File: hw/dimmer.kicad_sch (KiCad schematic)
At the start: 40 parts, among them J4 Screw_Terminal_01x02, Q10 MMBT3904, Q11 MMBT3906, Q13 IPN80R900P7, Q14 IPN80R900P7, Q9 MMBT3904, U2 PC817XI, U3 H11L1SR2M, U4 PC817XI

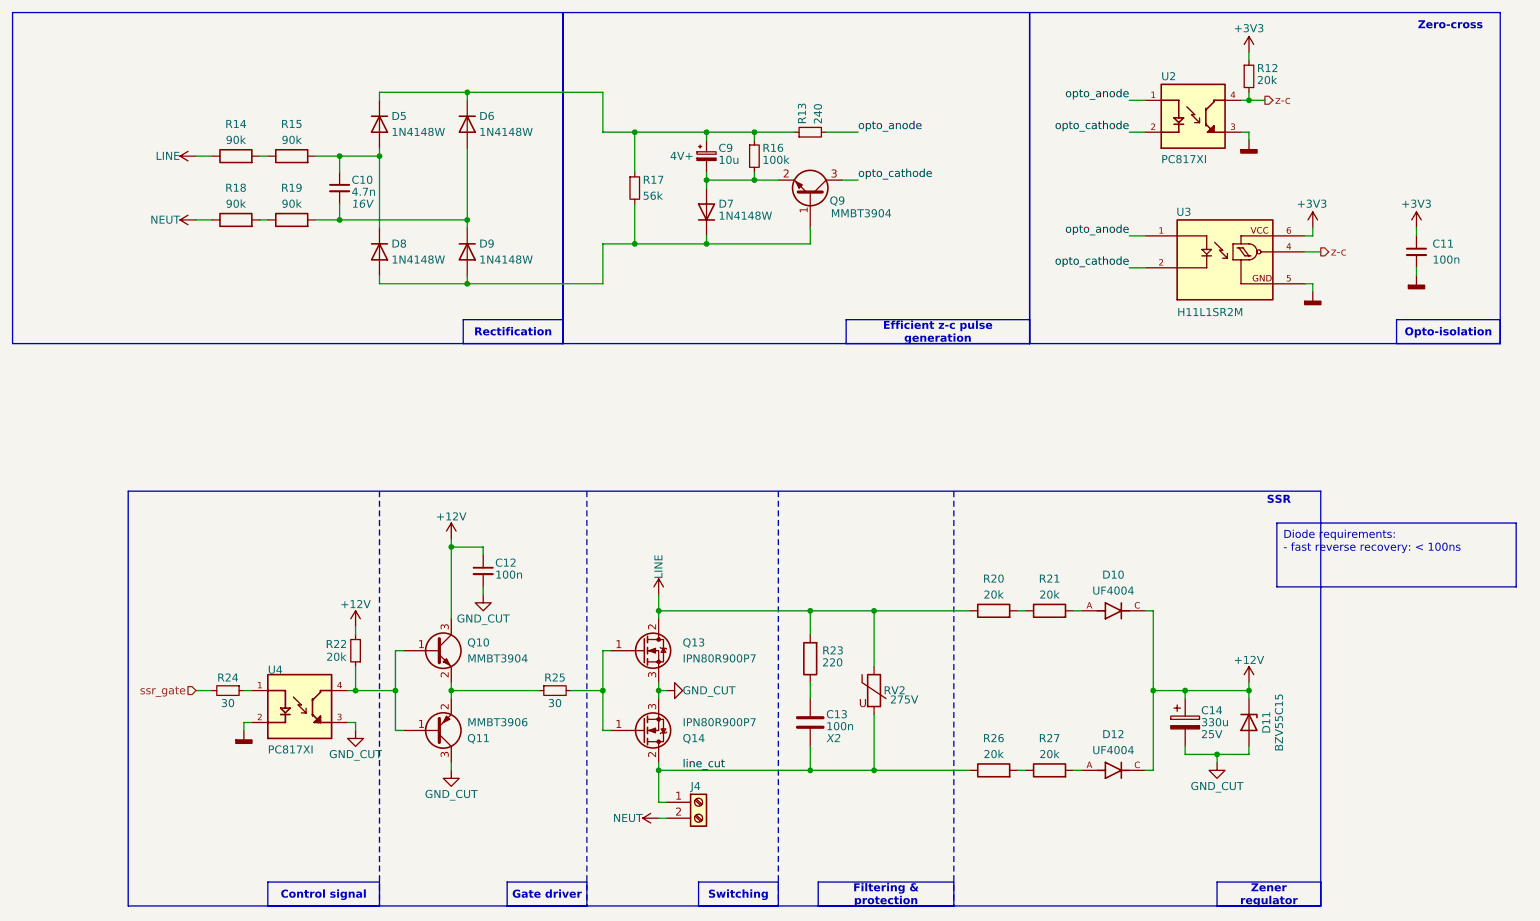
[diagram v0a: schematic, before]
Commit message: V2.0 (#2)
* **Hardware & Mechanical Design**
  * Updated design files and exports.
  * Split chassis and top plate into variants.
  * Changed enclosure folder structure.
  * Hid alignment/dimension layers; removed duplicate models.
  * Added mechanical parts and notes to schematics.

* **Firmware**
  * Updated firmware and added new versions.
  * Introduced firmware variants and consolidated them into packages.
  * Added common.yaml.
  * Moved effects out of packages.

* **Project Structure & Tooling**
  * Added BOM exports and fixed script permissions.
  * Updated and cleaned export folders.
  * Added ESPHome auto-generated `.gitignore`.
  * Fixed included libraries.
  * Miscellaneous corrections, reviews, merges, and cleanup commits.

* **Documentation & README**
  * Multiple revisions for clarity, formatting, structure, and consistency.
  * Added safety warnings for mains voltage operation.
  * Updated table of contents, badges, links, images, and repository structure sections.
  * Added roadmap, split release and change logs, reformatted release log.
  * Added links to schematic, PCB, BOMs, and iBOM.
  * Added additional documentation files.

* **Images, Photos & Media**
  * Updated, renamed, resized, and reformatted images.
  * Improved README image layout (width adjustments, centering, reduced size).
  * Added photos and screenshots across README and sub-readmes.
  * Added animations and animation exports; removed obsolete images.
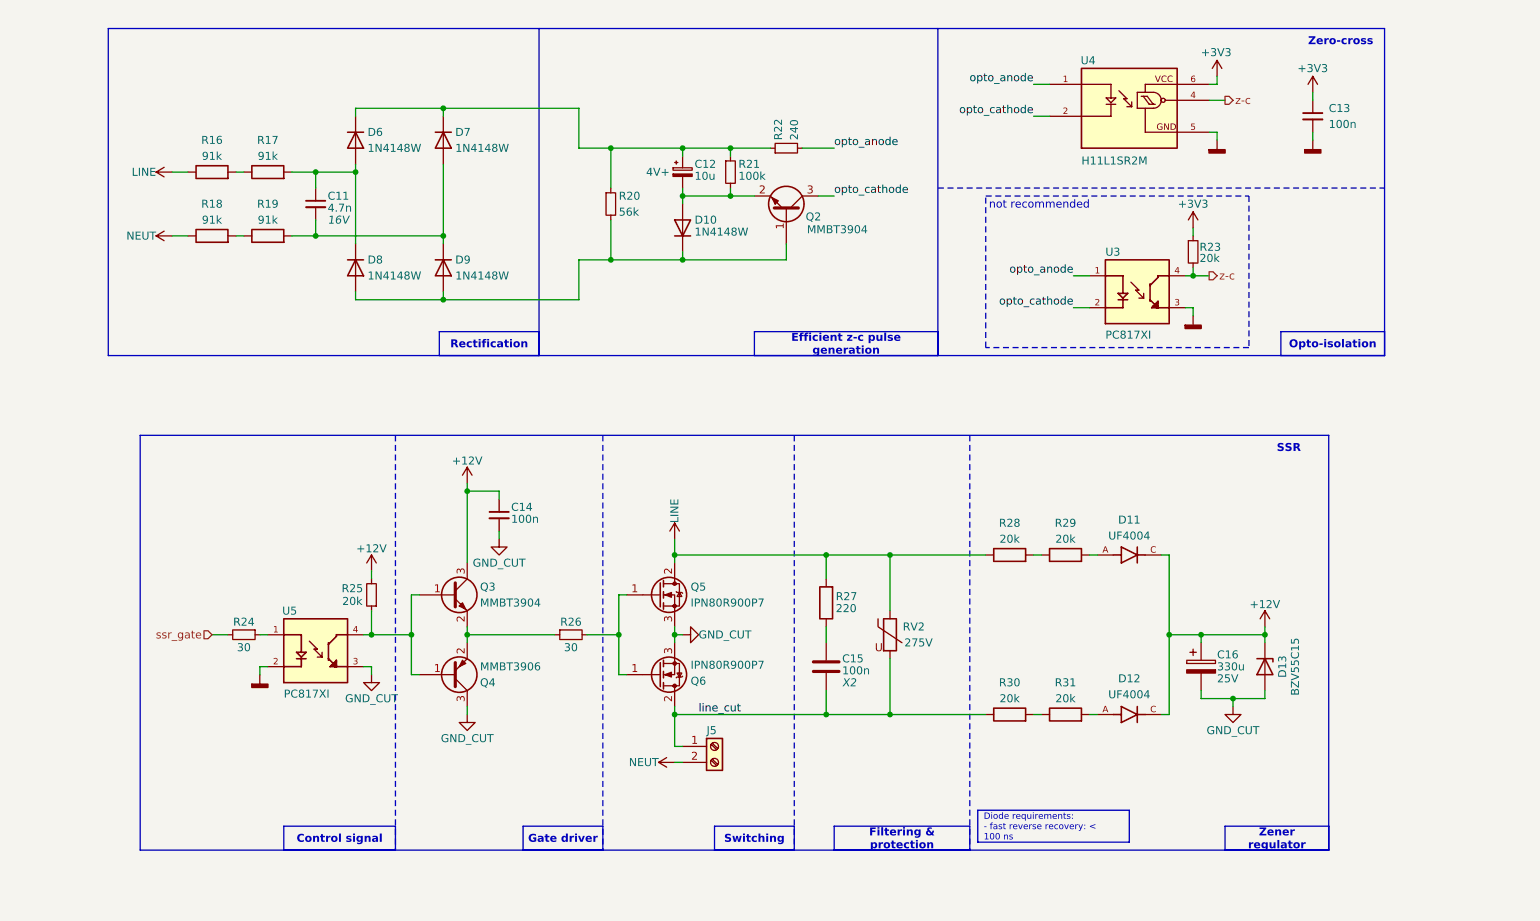
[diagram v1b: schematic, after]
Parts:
- R16: renamed from R14; value 90k -> 91k
- R17: renamed from R15; value 90k -> 91k
- R18, R19: value 90k -> 91k
- renumbered C10 to C11, C9 to C12, C11 to C13, C12 to C14, C13 to C15, C14 to C16, D7 to D10, D10 to D11, D11 to D13, D5 to D6, D6 to D7, J4 to J5, Q9 to Q2, Q10 to Q3, Q11 to Q4, Q13 to Q5, Q14 to Q6, R17 to R20, R16 to R21, R13 to R22, R12 to R23, R22 to R25, R25 to R26, R23 to R27, R20 to R28, R21 to R29, R26 to R30, R27 to R31, U2 to U3, U3 to U4, U4 to U5
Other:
- note added: "not recommended"
- title: LEDDs -> Dimmer
- moved on the sheet: C11, C12, C13, C14, C15, C16, D10, D11, D12, D13, D6, D7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
